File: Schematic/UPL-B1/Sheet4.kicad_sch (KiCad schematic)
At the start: 61 parts, among them P40 TestPoint

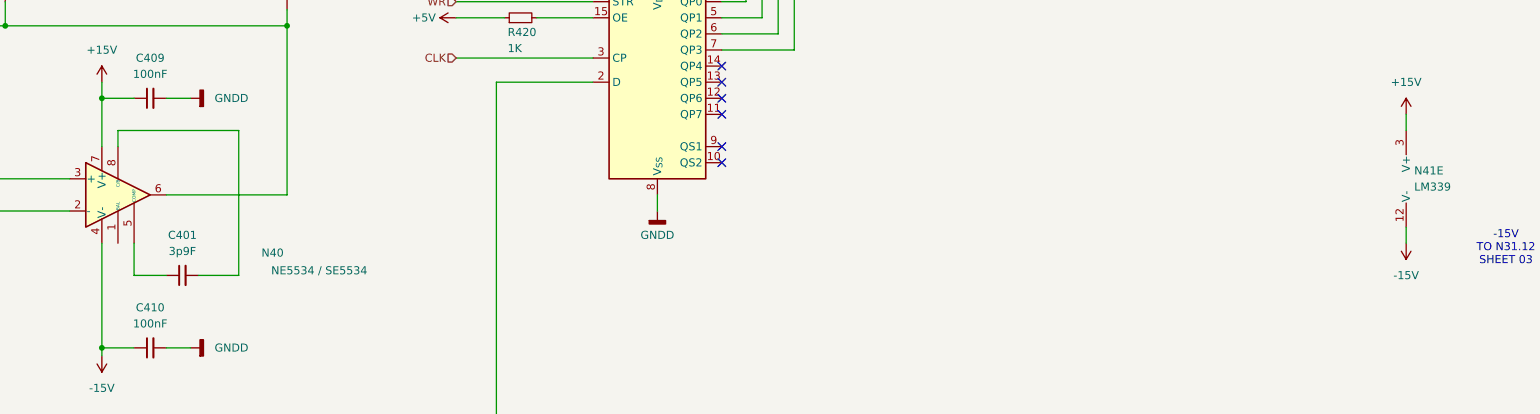
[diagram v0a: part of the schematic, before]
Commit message: ERC fixes.
- Power flags added for power nets "hanging" off resistors.
- Add missing NC-markers for intentionally unconnected parts
- Fix -15V bridge between circuits on S4/S3
- Add +5 to /CLR of DAC
- Use non-hierachical labels on main sheet.
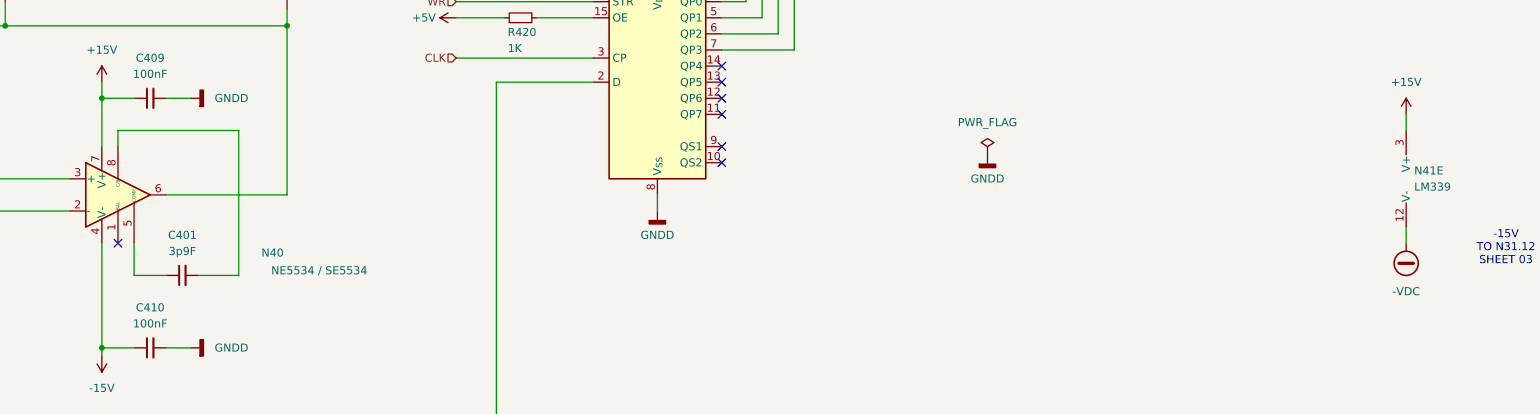
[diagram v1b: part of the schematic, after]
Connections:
- net -15V: no longer N41.12 (V-)
- new net -VDC: N41.12 (V-)
- no-connect marks 6 -> 7
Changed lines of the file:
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@@
 	)
 	(no_connect
+		(at 172.72 236.22)
+	)
+	(no_connect
 		(at 267.97 223.52)
 	)
@@
 	)
 	(symbol
-		(lib_id "power:+5V")
-		(at 375.92 236.22 180)
-		(unit 1)
-		(exclude_from_sim no)
-		(in_bom yes)
-		(on_board yes)
-		(dnp no)
-		(fields_autoplaced yes)
-		(property "Reference" "#PWR019"
-			(at 375.92 232.41 0)
-			(effects
-				(font
-					(size 1.27 1.27)
-				)
-				(hide yes)
-			)
-		)
-		(property "Value" "-15V"
-			(at 375.92 241.3 0)
-			(effects
-				(font
-					(size 1.27 1.27)
-				)
-			)
-		)
-		(property "Footprint" ""
-			(at 375.92 236.22 0)
-			(effects
-				(font
-					(size 1.27 1.27)
-				)
-				(hide yes)
-			)
-		)
-		(property "Datasheet" ""
-			(at 375.92 236.22 0)
-			(effects
-				(font
-					(size 1.27 1.27)
-				)
-				(hide yes)
-			)
-		)
-		(property "Description" "Power symbol creates a global label with name \"+5V\""
-			(at 375.92 236.22 0)
-			(effects
-				(font
-					(size 1.27 1.27)
-				)
-				(hide yes)
-			)
-		)
-		(pin "1"
-		)
-		(instances
-			(project "UPL_B1"
-				(path "/812de09b-8b67-463d-bf96-bb3aeeb1ed8d/5c1faa4b-2306-4f0f-97e7-c76d1ee80adb"
-					(reference "#PWR019")
-					(unit 1)
-				)
-			)
-		)
-	)
-	(symbol
 		(lib_id "Transistor_BJT:Q_PNP_BCE")
 		(at 81.28 49.53 0)
@@
 	)
 	(symbol
+		(lib_id "power:-VDC")
+		(at 375.92 236.22 180)
+		(unit 1)
+		(exclude_from_sim no)
+		(in_bom yes)
+		(on_board yes)
+		(dnp no)
+		(fields_autoplaced yes)
+		(property "Reference" "#PWR07"
+			(at 375.92 233.68 0)
+			(effects
+				(font
+					(size 1.27 1.27)
+				)
+				(hide yes)
+			)
+		)
+		(property "Value" "-VDC"
+			(at 375.92 243.84 0)
+			(effects
+				(font
+					(size 1.27 1.27)
+				)
+			)
+		)
+		(property "Footprint" ""
+			(at 375.92 236.22 0)
+			(effects
+				(font
+					(size 1.27 1.27)
+				)
+				(hide yes)
+			)
+		)
+		(property "Datasheet" ""
+			(at 375.92 236.22 0)
+			(effects
+				(font
+					(size 1.27 1.27)
+				)
+				(hide yes)
+			)
+		)
+		(property "Description" "Power symbol creates a global label with name \"-VDC\""
+			(at 375.92 236.22 0)
+			(effects
+				(font
+					(size 1.27 1.27)
+				)
+				(hide yes)
+			)
+		)
+		(pin "1"
+		)
+		(instances
+			(project "UPL-B1"
+				(path "/812de09b-8b67-463d-bf96-bb3aeeb1ed8d/5c1faa4b-2306-4f0f-97e7-c76d1ee80adb"
+					(reference "#PWR07")
+					(unit 1)
+				)
+			)
+		)
+	)
+	(symbol
 		(lib_id "power:GNDD")
 		(at 184.15 252.73 90)
@@
 	)
 	(symbol
+		(lib_id "power:PWR_FLAG")
+		(at 309.88 222.25 0)
+		(unit 1)
+		(exclude_from_sim no)
+		(in_bom yes)
+		(on_board yes)
+		(dnp no)
+		(fields_autoplaced yes)
+		(property "Reference" "#FLG02"
+			(at 309.88 220.345 0)
+			(effects
+				(font
+					(size 1.27 1.27)
+				)
+				(hide yes)
+			)
+		)
+		(property "Value" "PWR_FLAG"
+			(at 309.88 217.17 0)
+			(effects
+				(font
+					(size 1.27 1.27)
+				)
+			)
+		)
+		(property "Footprint" ""
+			(at 309.88 222.25 0)
+			(effects
+				(font
+					(size 1.27 1.27)
+				)
+				(hide yes)
+			)
+		)
+		(property "Datasheet" "~"
+			(at 309.88 222.25 0)
+			(effects
+				(font
+					(size 1.27 1.27)
+				)
+				(hide yes)
+			)
+		)
+		(property "Description" "Special symbol for telling ERC where power comes from"
+			(at 309.88 222.25 0)
+			(effects
+				(font
+					(size 1.27 1.27)
+				)
+				(hide yes)
+			)
+		)
+		(pin "1"
+		)
+		(instances
+			(project ""
+				(path "/812de09b-8b67-463d-bf96-bb3aeeb1ed8d/5c1faa4b-2306-4f0f-97e7-c76d1ee80adb"
+					(reference "#FLG02")
+					(unit 1)
+				)
+			)
+		)
+	)
+	(symbol
 		(lib_id "Device:R_Small")
 		(at 163.83 90.17 0)
@@
 					(unit 1)
 				)
+			)
+		)
+	)
+	(symbol
+		(lib_id "power:GNDD")
+		(at 309.88 222.25 0)
+		(unit 1)
+		(exclude_from_sim no)
+		(in_bom yes)
+		(on_board yes)
+		(dnp no)
+		(fields_autoplaced yes)
+		(property "Reference" "#PWR01"
+			(at 309.88 228.6 0)
+			(effects
+				(font
+					(size 1.27 1.27)
+				)
+				(hide yes)
+			)
+		)
+		(property "Value" "GNDD"
+			(at 309.88 226.06 0)
+			(effects
+				(font
+					(size 1.27 1.27)
+				)
+			)
+		)
+		(property "Footprint" ""
+			(at 309.88 222.25 0)
+			(effects
+				(font
+					(size 1.27 1.27)
+				)
+				(hide yes)
+			)
+		)
+		(property "Datasheet" ""
+			(at 309.88 222.25 0)
+			(effects
+				(font
+					(size 1.27 1.27)
+				)
+				(hide yes)
+			)
+		)
+		(property "Description" "Power symbol creates a global label with name \"GNDD\" , digital ground"
+			(at 309.88 222.25 0)
+			(effects
+				(font
+					(size 1.27 1.27)
+				)
+				(hide yes)
+			)
+		)
+		(pin "1"
+		)
+		(instances
+			(project ""
+				(path "/812de09b-8b67-463d-bf96-bb3aeeb1ed8d/5c1faa4b-2306-4f0f-97e7-c76d1ee80adb"
+					(reference "#PWR01")
+					(unit 1)
+				)

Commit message: Minor readability changes
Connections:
- net +5V: no longer R410.1
- new net +5VA: R410.1
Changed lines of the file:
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@@
 	(wire
 		(pts
+			(xy 24.13 227.33) (xy 24.13 231.14)
+		)
+		(stroke
+			(width 0)
+			(type default)
+		)
+	)
+	(wire
+		(pts
 			(xy 356.87 93.98) (xy 359.41 93.98)
 		)
@@
 	(wire
 		(pts
+			(xy 24.13 231.14) (xy 26.67 231.14)
+		)
+		(stroke
+			(width 0)
+			(type default)
+		)
+	)
+	(wire
+		(pts
 			(xy 267.97 203.2) (xy 276.86 203.2)
 		)
@@
 	(wire
 		(pts
-			(xy 25.4 231.14) (xy 26.67 231.14)
-		)
-		(stroke
-			(width 0)
-			(type default)
-		)
-	)
-	(wire
-		(pts
 			(xy 144.78 198.12) (xy 144.78 201.93)
 		)
@@
 	)
 	(symbol
-		(lib_id "power:+5V")
-		(at 25.4 231.14 90)
-		(unit 1)
-		(exclude_from_sim no)
-		(in_bom yes)
-		(on_board yes)
-		(dnp no)
-		(fields_autoplaced yes)
-		(property "Reference" "#PWR025"
-			(at 29.21 231.14 0)
-			(effects
-				(font
-					(size 1.27 1.27)
-				)
-				(hide yes)
-			)
-		)
-		(property "Value" "+5V"
-			(at 21.59 231.1401 90)
-			(effects
-				(font
-					(size 1.27 1.27)
-				)
-				(justify left)
-			)
-		)
-		(property "Footprint" ""
-			(at 25.4 231.14 0)
-			(effects
-				(font
-					(size 1.27 1.27)
-				)
-				(hide yes)
-			)
-		)
-		(property "Datasheet" ""
-			(at 25.4 231.14 0)
-			(effects
-				(font
-					(size 1.27 1.27)
-				)
-				(hide yes)
-			)
-		)
-		(property "Description" "Power symbol creates a global label with name \"+5V\""
-			(at 25.4 231.14 0)
-			(effects
-				(font
-					(size 1.27 1.27)
-				)
-				(hide yes)
-			)
-		)
-		(pin "1"
-		)
-		(instances
-			(project "UPL_B1"
-				(path "/812de09b-8b67-463d-bf96-bb3aeeb1ed8d/5c1faa4b-2306-4f0f-97e7-c76d1ee80adb"
-					(reference "#PWR025")
-					(unit 1)
-				)
-			)
-		)
-	)
-	(symbol
 		(lib_id "Device:R_Small")
 		(at 96.52 49.53 90)
@@
 					(unit 1)
 				)
+			)
+		)
+	)
+	(symbol
+		(lib_id "power:+5VA")
+		(at 24.13 227.33 0)
+		(unit 1)
+		(exclude_from_sim no)
+		(in_bom yes)
+		(on_board yes)
+		(dnp no)
+		(fields_autoplaced yes)
+		(property "Reference" "#PWR020"
+			(at 24.13 231.14 0)
+			(effects
+				(font
+					(size 1.27 1.27)
+				)
+				(hide yes)
+			)
+		)
+		(property "Value" "+5VA"
+			(at 24.13 222.25 0)
+			(effects
+				(font
+					(size 1.27 1.27)
+				)
+			)
+		)
+		(property "Footprint" ""
+			(at 24.13 227.33 0)
+			(effects
+				(font
+					(size 1.27 1.27)
+				)
+				(hide yes)
+			)
+		)
+		(property "Datasheet" ""
+			(at 24.13 227.33 0)
+			(effects
+				(font
+					(size 1.27 1.27)
+				)
+				(hide yes)
+			)
+		)
+		(property "Description" "Power symbol creates a global label with name \"+5VA\""
+			(at 24.13 227.33 0)
+			(effects
+				(font
+					(size 1.27 1.27)
+				)
+				(hide yes)
+			)
+		)
+		(pin "1"
+		)
+		(instances
+			(project "UPL-B1"
+				(path "/812de09b-8b67-463d-bf96-bb3aeeb1ed8d/5c1faa4b-2306-4f0f-97e7-c76d1ee80adb"
+					(reference "#PWR020")
+					(unit 1)
+				)
